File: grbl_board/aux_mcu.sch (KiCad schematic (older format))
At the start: 50 parts, among them J17 USB_B, J18 ICSP, Q5 BSS127S, Q6 BSS127S, Q7 BSS127S, SW2 SW_Push, U25 FT231XS, U26 40106, U27 74LS155, U28 ATmega328P-AU, U29 74LS153, U30 74LS153, Y2 16M

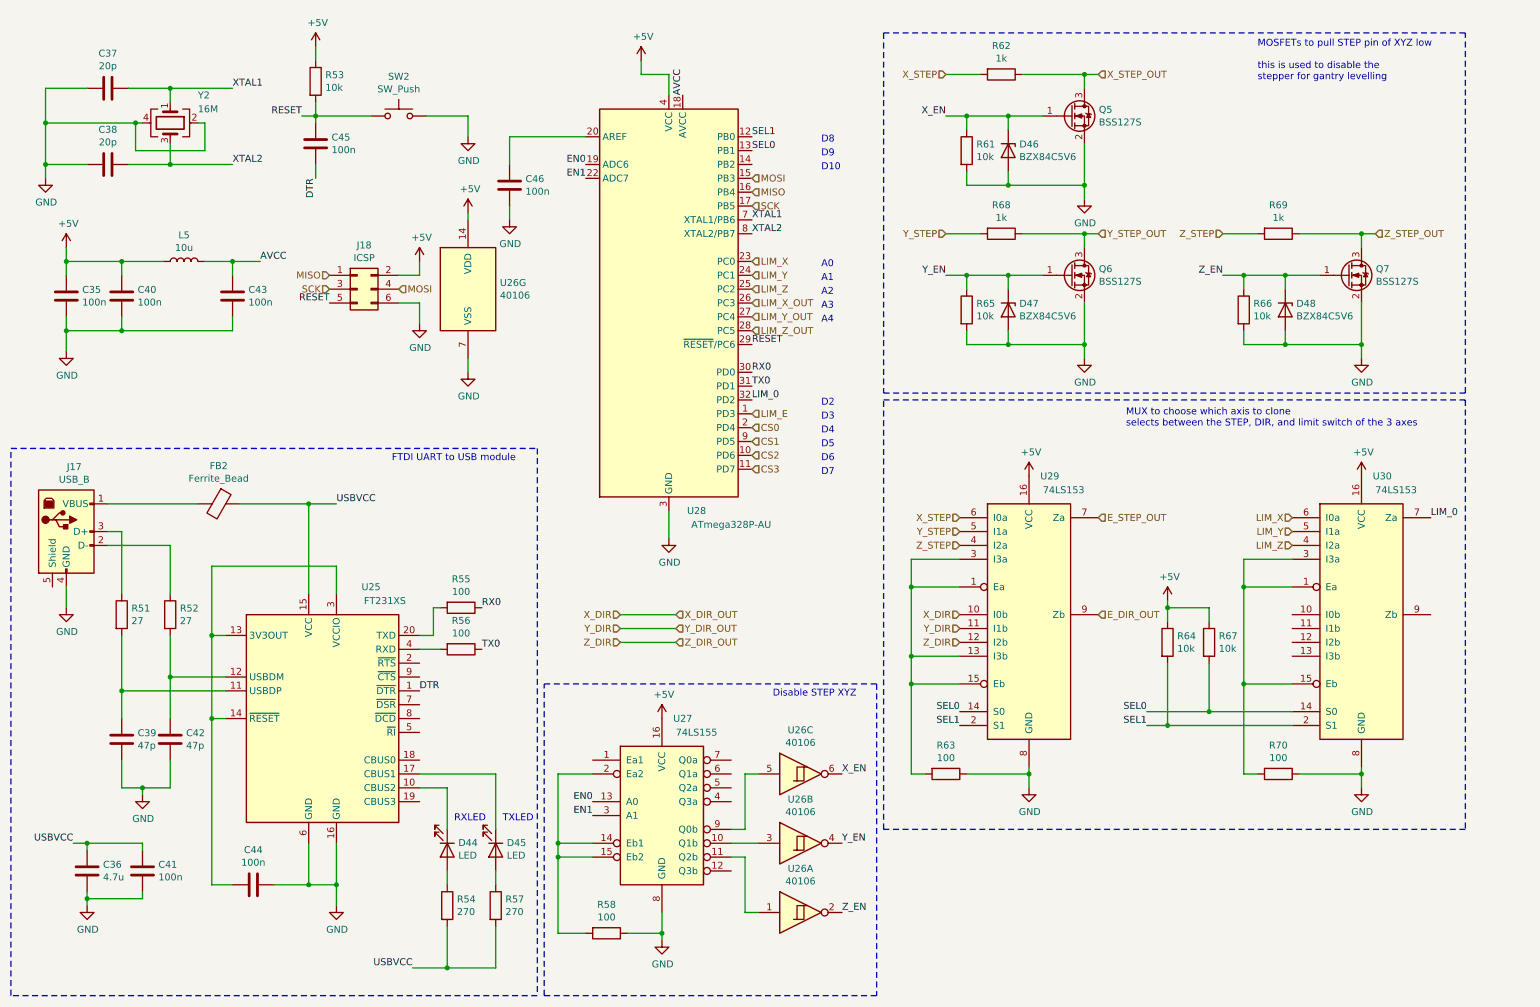
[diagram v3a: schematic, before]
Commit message: fixed limit switch disconnect issue
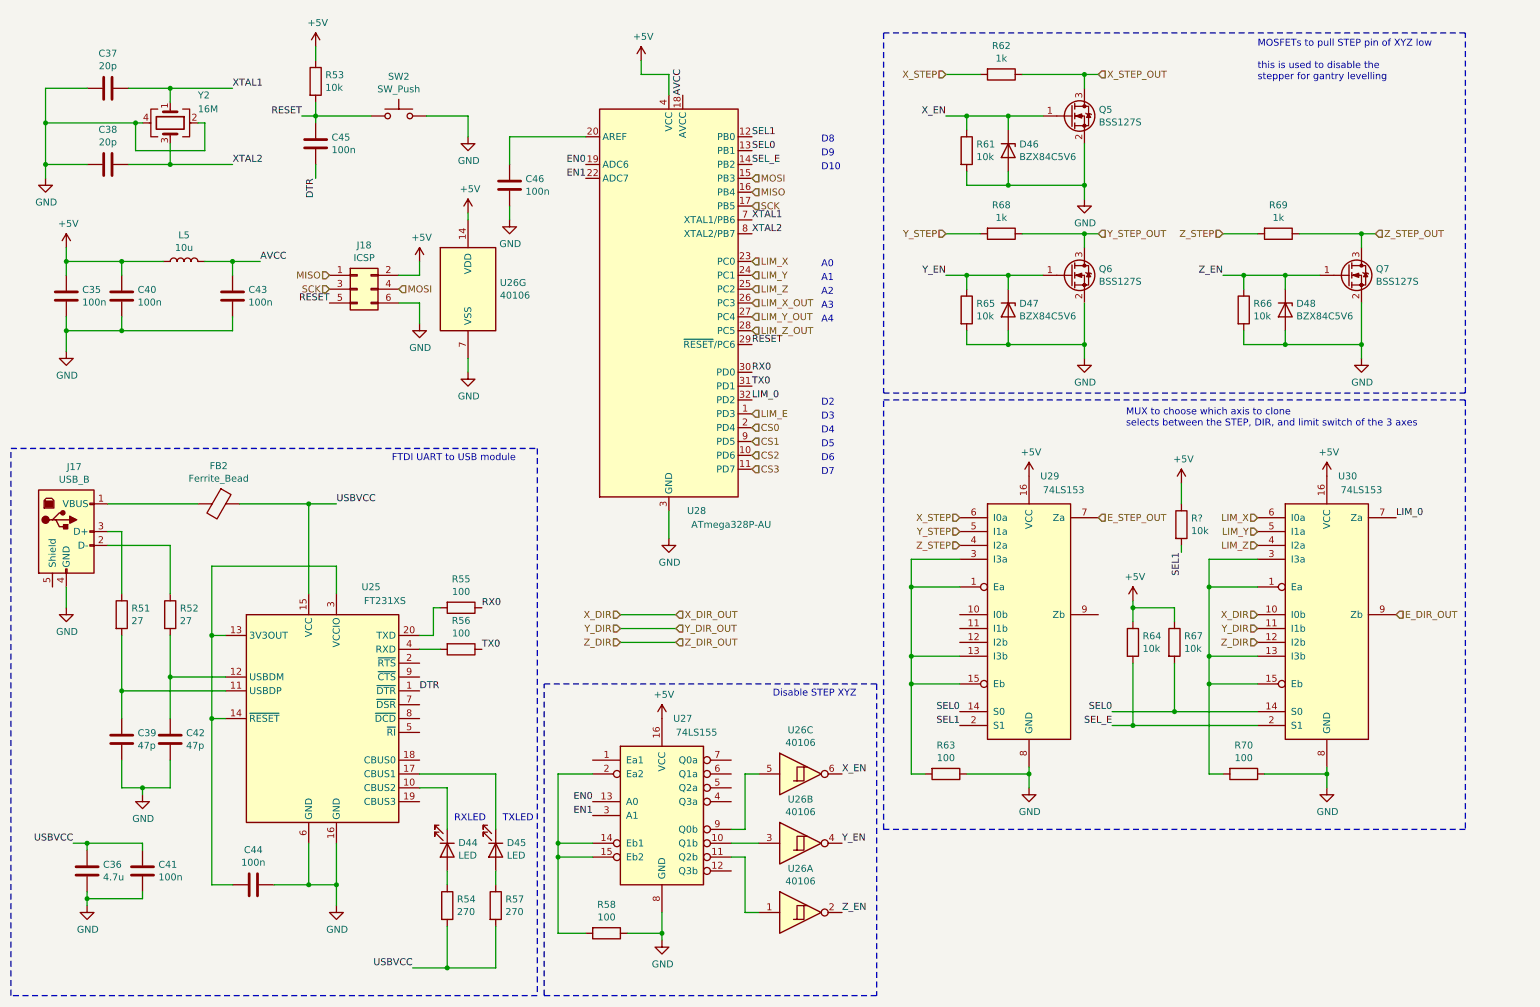
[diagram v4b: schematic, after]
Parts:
- added R?: 10k, Resistor_SMD:R_0805_2012Metric_Pad1.15x1.40mm_HandSolder, symbol Device:R
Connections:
- net +5V: now also R?.1
- net E_DIR_OUT: now also U30.9 (Zb); no longer U29.9 (Zb)
- net SEL1: now also R?.2; no longer R64.2, U30.2 (S1)
- net X_DIR: now also U30.10 (I0b); no longer U29.10 (I0b)
- net Y_DIR: now also U30.11 (I1b); no longer U29.11 (I1b)
- net Z_DIR: now also U30.12 (I2b); no longer U29.12 (I2b)
- net SEL_E: now reaches U28.14 (PB2)
- net SEL_E: now also R64.2, U30.2 (S1)
- net at R70.2, U30.1 (Ea), U30.15 (Eb)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: now also U30.13 (I3b)
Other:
- moved on the sheet: R64, R67, R70, U30
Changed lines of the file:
@@
 	1    0    0    -1
 $EndComp
-Text Label 10800 4200 0    50   ~ 0
+Text Label 10550 4200 0    50   ~ 0
 LIM_0
 Text Label 7400 5600 2    50   ~ 0
@@
 Wire Notes Line
 	4400 5400 6800 5400
-Connection ~ 9200 5600
-Connection ~ 8900 5700
+Connection ~ 8950 5600
+Connection ~ 8650 5700
 $Comp
 L Device:R R67
 U 1 1 61E49973
-P 9200 5100
-F 0 "R67" H 9270 5146 50  0000 L CNN
-F 1 "10k" H 9270 5055 50  0000 L CNN
-F 2 "Resistor_SMD:R_0805_2012Metric_Pad1.15x1.40mm_HandSolder" V 9130 5100 50  0001 C CNN
-F 3 "https://www.yageo.com/upload/media/product/productsearch/datasheet/rchip/PYu-RC_Group_51_RoHS_L_11.pdf" H 9200 5100 50  0001 C CNN
-F 4 "311-10KARCT-ND" H 9200 5100 50  0001 C CNN "Digikey Part No."
-	1    9200 5100
-	1    0    0    -1
-$EndComp
-Wire Wire Line
-	9200 5600 9200 5250
-Wire Wire Line
-	9200 5600 8750 5600
-Wire Wire Line
-	9200 5600 9800 5600
-Wire Wire Line
-	8900 4850 9200 4850
-Connection ~ 8900 4850
-Wire Wire Line
-	8900 4800 8900 4850
-Wire Wire Line
-	8900 4850 8900 4950
-Wire Wire Line
-	9200 4850 9200 4950
-Wire Wire Line
-	8900 5700 8900 5250
-Wire Wire Line
-	8750 5700 8900 5700
-Wire Wire Line
-	9800 5700 8900 5700
+P 8950 5100
+F 0 "R67" H 9020 5146 50  0000 L CNN
+F 1 "10k" H 9020 5055 50  0000 L CNN
+F 2 "Resistor_SMD:R_0805_2012Metric_Pad1.15x1.40mm_HandSolder" V 8880 5100 50  0001 C CNN
+F 3 "https://www.yageo.com/upload/media/product/productsearch/datasheet/rchip/PYu-RC_Group_51_RoHS_L_11.pdf" H 8950 5100 50  0001 C CNN
+F 4 "311-10KARCT-ND" H 8950 5100 50  0001 C CNN "Digikey Part No."
+	1    8950 5100
+	1    0    0    -1
+$EndComp
+Wire Wire Line
+	8950 5600 8950 5250
+Wire Wire Line
+	8950 5600 8500 5600
+Wire Wire Line
+	8950 5600 9550 5600
+Wire Wire Line
+	8650 4850 8950 4850
+Connection ~ 8650 4850
+Wire Wire Line
+	8650 4800 8650 4850
+Wire Wire Line
+	8650 4850 8650 4950
+Wire Wire Line
+	8950 4850 8950 4950
+Wire Wire Line
+	8650 5700 8650 5250
+Wire Wire Line
+	8500 5700 8650 5700
+Wire Wire Line
+	9550 5700 8650 5700
 $Comp
 L power:+5V #PWR099
 U 1 1 61E499A2
-P 8900 4800
-F 0 "#PWR099" H 8900 4650 50  0001 C CNN
-F 1 "+5V" H 8915 4973 50  0000 C CNN
-F 2 "" H 8900 4800 50  0001 C CNN
-F 3 "" H 8900 4800 50  0001 C CNN
-	1    8900 4800
+P 8650 4800
+F 0 "#PWR099" H 8650 4650 50  0001 C CNN
+F 1 "+5V" H 8665 4973 50  0000 C CNN
+F 2 "" H 8650 4800 50  0001 C CNN
+F 3 "" H 8650 4800 50  0001 C CNN
+	1    8650 4800
 	1    0    0    -1
 $EndComp
@@
 L Device:R R64
 U 1 1 61E499A8
-P 8900 5100
-F 0 "R64" H 8970 5146 50  0000 L CNN
-F 1 "10k" H 8970 5055 50  0000 L CNN
-F 2 "Resistor_SMD:R_0805_2012Metric_Pad1.15x1.40mm_HandSolder" V 8830 5100 50  0001 C CNN
-F 3 "https://www.yageo.com/upload/media/product/productsearch/datasheet/rchip/PYu-RC_Group_51_RoHS_L_11.pdf" H 8900 5100 50  0001 C CNN
-F 4 "311-10KARCT-ND" H 8900 5100 50  0001 C CNN "Digikey Part No."
-	1    8900 5100
+P 8650 5100
+F 0 "R64" H 8720 5146 50  0000 L CNN
+F 1 "10k" H 8720 5055 50  0000 L CNN
+F 2 "Resistor_SMD:R_0805_2012Metric_Pad1.15x1.40mm_HandSolder" V 8580 5100 50  0001 C CNN
+F 3 "https://www.yageo.com/upload/media/product/productsearch/datasheet/rchip/PYu-RC_Group_51_RoHS_L_11.pdf" H 8650 5100 50  0001 C CNN
+F 4 "311-10KARCT-ND" H 8650 5100 50  0001 C CNN "Digikey Part No."
+	1    8650 5100
 	1    0    0    -1
 $EndComp
 Text HLabel 8400 4200 2    50   Input ~ 0
 E_STEP_OUT
-Text Label 8750 5600 2    50   ~ 0
+Text Label 8500 5600 2    50   ~ 0
 SEL0
-Text Label 8750 5700 2    50   ~ 0
-SEL1
-Wire Wire Line
-	10300 6000 10300 6050
-Connection ~ 9450 4700
-Wire Wire Line
-	9450 4500 9450 4700
-Wire Wire Line
-	9800 4500 9450 4500
-Connection ~ 9450 5400
-Wire Wire Line
-	9800 5400 9450 5400
-Wire Wire Line
-	9450 4700 9800 4700
-Wire Wire Line
-	9450 6050 9450 5400
-Text HLabel 9800 4400 0    50   Input ~ 0
+Wire Wire Line
+	10050 6000 10050 6050
+Connection ~ 9200 4700
+Wire Wire Line
+	9200 4500 9200 4700
+Wire Wire Line
+	9550 4500 9200 4500
+Connection ~ 9200 5400
+Wire Wire Line
+	9550 5400 9200 5400
+Wire Wire Line
+	9200 4700 9550 4700
+Wire Wire Line
+	9200 6050 9200 5400
+Text HLabel 9550 4400 0    50   Input ~ 0
 LIM_Z
-Text HLabel 9800 4300 0    50   Input ~ 0
+Text HLabel 9550 4300 0    50   Input ~ 0
 LIM_Y
-Text HLabel 9800 4200 0    50   Input ~ 0
+Text HLabel 9550 4200 0    50   Input ~ 0
 LIM_X
 $Comp
 L 74xx:74LS153 U30
 U 1 1 61E49967
-P 10300 4900
-F 0 "U30" H 10450 5900 50  0000 C CNN
-F 1 "74LS153" H 10550 5800 50  0000 C CNN
-F 2 "Package_SO:SOIC-16_3.9x9.9mm_P1.27mm" H 10300 4900 50  0001 C CNN
-F 3 "http://www.ti.com/lit/gpn/sn74LS153" H 10300 4900 50  0001 C CNN
-F 4 "296-3653-5-ND" H 10300 4900 50  0001 C CNN "Digikey Part No."
-	1    10300 4900
-	1    0    0    -1
-$EndComp
-Text HLabel 8400 4900 2    50   Input ~ 0
-E_DIR_OUT
+P 10050 4900
+F 0 "U30" H 10200 5900 50  0000 C CNN
+F 1 "74LS153" H 10300 5800 50  0000 C CNN
+F 2 "Package_SO:SOIC-16_3.9x9.9mm_P1.27mm" H 10050 4900 50  0001 C CNN
+F 3 "http://www.ti.com/lit/gpn/sn74LS153" H 10050 4900 50  0001 C CNN
+F 4 "296-3653-5-ND" H 10050 4900 50  0001 C CNN "Digikey Part No."
+	1    10050 4900
+	1    0    0    -1
+$EndComp
 Wire Wire Line
 	7900 6050 7900 6150
@@
 	1    0    0    -1
 $EndComp
-Text HLabel 7400 5100 0    50   Input ~ 0
-Z_DIR
-Text HLabel 7400 5000 0    50   Input ~ 0
-Y_DIR
-Text HLabel 7400 4900 0    50   Input ~ 0
-X_DIR
 Text HLabel 7400 4400 0    50   Input ~ 0
 Z_STEP
@@
 L power:+5V #PWR0102
 U 1 1 61E8DDDC
-P 10300 3900
-F 0 "#PWR0102" H 10300 3750 50  0001 C CNN
-F 1 "+5V" H 10315 4073 50  0000 C CNN
-F 2 "" H 10300 3900 50  0001 C CNN
-F 3 "" H 10300 3900 50  0001 C CNN
-	1    10300 3900
-	1    0    0    -1
-$EndComp
-Wire Wire Line
-	9450 4700 9450 5400
-Connection ~ 10300 6050
+P 10050 3900
+F 0 "#PWR0102" H 10050 3750 50  0001 C CNN
+F 1 "+5V" H 10065 4073 50  0000 C CNN
+F 2 "" H 10050 3900 50  0001 C CNN
+F 3 "" H 10050 3900 50  0001 C CNN
+	1    10050 3900
+	1    0    0    -1
+$EndComp
+Wire Wire Line
+	9200 4700 9200 5200
+Connection ~ 10050 6050
 $Comp
 L power:GND #PWR0103
 U 1 1 61E4997C
-P 10300 6150
-F 0 "#PWR0103" H 10300 5900 50  0001 C CNN
-F 1 "GND" H 10305 5977 50  0000 C CNN
-F 2 "" H 10300 6150 50  0001 C CNN
-F 3 "" H 10300 6150 50  0001 C CNN
-	1    10300 6150
+P 10050 6150
+F 0 "#PWR0103" H 10050 5900 50  0001 C CNN
+F 1 "GND" H 10055 5977 50  0000 C CNN
+F 2 "" H 10050 6150 50  0001 C CNN
+F 3 "" H 10050 6150 50  0001 C CNN
+	1    10050 6150
 	1    0    0    -1
 $EndComp
@@
 L Device:R R70
 U 1 1 61E4998E
-P 9700 6050
-F 0 "R70" V 9493 6050 50  0000 C CNN
-F 1 "100" V 9584 6050 50  0000 C CNN
-F 2 "Resistor_SMD:R_0603_1608Metric_Pad0.98x0.95mm_HandSolder" V 9630 6050 50  0001 C CNN
-F 3 "https://www.yageo.com/upload/media/product/productsearch/datasheet/rchip/PYu-RC_Group_51_RoHS_L_11.pdf" H 9700 6050 50  0001 C CNN
-F 4 "311-100GRCT-ND" H 9700 6050 50  0001 C CNN "Digikey Part No."
-	1    9700 6050
+P 9450 6050
+F 0 "R70" V 9243 6050 50  0000 C CNN
+F 1 "100" V 9334 6050 50  0000 C CNN
+F 2 "Resistor_SMD:R_0603_1608Metric_Pad0.98x0.95mm_HandSolder" V 9380 6050 50  0001 C CNN
+F 3 "https://www.yageo.com/upload/media/product/productsearch/datasheet/rchip/PYu-RC_Group_51_RoHS_L_11.pdf" H 9450 6050 50  0001 C CNN
+F 4 "311-100GRCT-ND" H 9450 6050 50  0001 C CNN "Digikey Part No."
+	1    9450 6050
 	0    1    1    0
 $EndComp
 Wire Wire Line
-	9550 6050 9450 6050
-Wire Wire Line
-	9850 6050 10300 6050
-Wire Wire Line
-	10300 6050 10300 6150
+	9300 6050 9200 6050
+Wire Wire Line
+	9600 6050 10050 6050
+Wire Wire Line
+	10050 6050 10050 6150
 Text Notes 9550 1050 0    50   ~ 0
 MOSFETs to pull STEP pin of XYZ low\n\nthis is used to disable the \nstepper for gantry levelling\n
@@
 Text Notes 8600 3550 0    50   ~ 0
 MUX to choose which axis to clone\nselects between the STEP, DIR, and limit switch of the 3 axes
+Text Label 5900 1650 0    50   ~ 0
+SEL_E
+Text Label 8500 5700 2    50   ~ 0
+SEL_E
+Text Label 9000 4450 3    50   ~ 0
+SEL1
+$Comp
+L power:+5V #PWR?
+U 1 1 6188BB6E
+P 9000 3950
+F 0 "#PWR?" H 9000 3800 50  0001 C CNN
+F 1 "+5V" H 9015 4123 50  0000 C CNN
+F 2 "" H 9000 3950 50  0001 C CNN
+F 3 "" H 9000 3950 50  0001 C CNN
+	1    9000 3950
+	1    0    0    -1
+$EndComp
+$Comp
+L Device:R R?
+U 1 1 6188BB75
+P 9000 4250
+F 0 "R?" H 9070 4296 50  0000 L CNN
+F 1 "10k" H 9070 4205 50  0000 L CNN
+F 2 "Resistor_SMD:R_0805_2012Metric_Pad1.15x1.40mm_HandSolder" V 8930 4250 50  0001 C CNN
+F 3 "https://www.yageo.com/upload/media/product/productsearch/datasheet/rchip/PYu-RC_Group_51_RoHS_L_11.pdf" H 9000 4250 50  0001 C CNN
+F 4 "311-10KARCT-ND" H 9000 4250 50  0001 C CNN "Digikey Part No."
+	1    9000 4250
+	1    0    0    -1
+$EndComp
+Wire Wire Line
+	9000 4100 9000 3950
+Wire Wire Line
+	9000 4450 9000 4400
+Text HLabel 9550 5100 0    50   Input ~ 0
+Z_DIR
+Text HLabel 9550 5000 0    50   Input ~ 0
+Y_DIR
+Text HLabel 9550 4900 0    50   Input ~ 0
+X_DIR
+Wire Wire Line
+	9550 5200 9200 5200
+Connection ~ 9200 5200
+Wire Wire Line
+	9200 5200 9200 5400
+Text HLabel 10550 4900 2    50   Input ~ 0
+E_DIR_OUT
 $EndSCHEMATC

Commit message: fixed copper fill
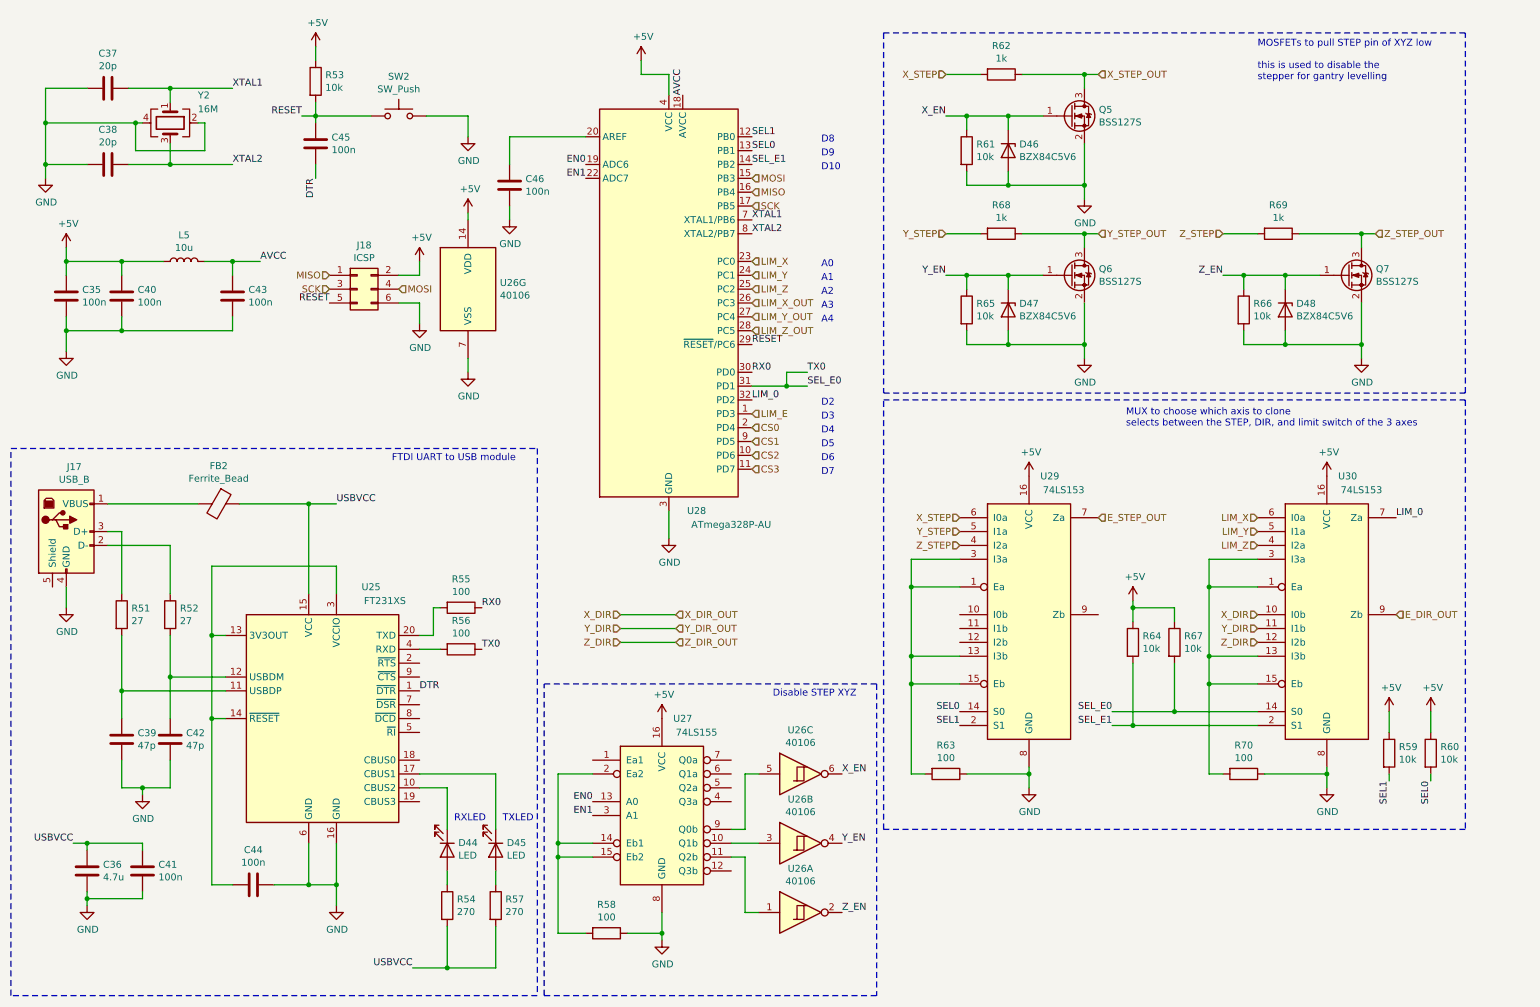
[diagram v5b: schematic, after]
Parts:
- added R60: 10k, Resistor_SMD:R_0805_2012Metric_Pad1.15x1.40mm_HandSolder, symbol Device:R
- gave numbers to parts that had none: 1
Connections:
- net +5V: now also R60.1
- net SEL0: now also R60.2; no longer R67.2, U30.14 (S0)
- net SEL_E renamed SEL_E1
- net TX0 renamed SEL_E0
- net SEL_E0: now also R67.2, U30.14 (S0)
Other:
- moved on the sheet: R59
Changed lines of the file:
@@
 Text Label 5900 3150 0    50   ~ 0
 RX0
-Text Label 5900 3250 0    50   ~ 0
+Text Label 6300 3150 0    50   ~ 0
 TX0
 Text Label 5900 2950 0    50   ~ 0
@@
 E_STEP_OUT
 Text Label 8500 5600 2    50   ~ 0
-SEL0
+SEL_E0
 Wire Wire Line
 	10050 6000 10050 6050
@@
 MUX to choose which axis to clone\nselects between the STEP, DIR, and limit switch of the 3 axes
 Text Label 5900 1650 0    50   ~ 0
-SEL_E
+SEL_E1
 Text Label 8500 5700 2    50   ~ 0
-SEL_E
-Text Label 9000 4450 3    50   ~ 0
+SEL_E1
+Text Label 10500 6100 3    50   ~ 0
 SEL1
 $Comp
-L power:+5V #PWR?
+L power:+5V #PWR0105
 U 1 1 6188BB6E
-P 9000 3950
-F 0 "#PWR?" H 9000 3800 50  0001 C CNN
-F 1 "+5V" H 9015 4123 50  0000 C CNN
-F 2 "" H 9000 3950 50  0001 C CNN
-F 3 "" H 9000 3950 50  0001 C CNN
-	1    9000 3950
-	1    0    0    -1
-$EndComp
-$Comp
-L Device:R R?
+P 10500 5600
+F 0 "#PWR0105" H 10500 5450 50  0001 C CNN
+F 1 "+5V" H 10515 5773 50  0000 C CNN
+F 2 "" H 10500 5600 50  0001 C CNN
+F 3 "" H 10500 5600 50  0001 C CNN
+	1    10500 5600
+	1    0    0    -1
+$EndComp
+$Comp
+L Device:R R59
 U 1 1 6188BB75
-P 9000 4250
-F 0 "R?" H 9070 4296 50  0000 L CNN
-F 1 "10k" H 9070 4205 50  0000 L CNN
-F 2 "Resistor_SMD:R_0805_2012Metric_Pad1.15x1.40mm_HandSolder" V 8930 4250 50  0001 C CNN
-F 3 "https://www.yageo.com/upload/media/product/productsearch/datasheet/rchip/PYu-RC_Group_51_RoHS_L_11.pdf" H 9000 4250 50  0001 C CNN
-F 4 "311-10KARCT-ND" H 9000 4250 50  0001 C CNN "Digikey Part No."
-	1    9000 4250
-	1    0    0    -1
-$EndComp
-Wire Wire Line
-	9000 4100 9000 3950
-Wire Wire Line
-	9000 4450 9000 4400
+P 10500 5900
+F 0 "R59" H 10570 5946 50  0000 L CNN
+F 1 "10k" H 10570 5855 50  0000 L CNN
+F 2 "Resistor_SMD:R_0805_2012Metric_Pad1.15x1.40mm_HandSolder" V 10430 5900 50  0001 C CNN
+F 3 "https://www.yageo.com/upload/media/product/productsearch/datasheet/rchip/PYu-RC_Group_51_RoHS_L_11.pdf" H 10500 5900 50  0001 C CNN
+F 4 "311-10KARCT-ND" H 10500 5900 50  0001 C CNN "Digikey Part No."
+	1    10500 5900
+	1    0    0    -1
+$EndComp
+Wire Wire Line
+	10500 5750 10500 5600
+Wire Wire Line
+	10500 6100 10500 6050
 Text HLabel 9550 5100 0    50   Input ~ 0
 Z_DIR
@@
 Text HLabel 10550 4900 2    50   Input ~ 0
 E_DIR_OUT
+Text Label 6300 3250 0    50   ~ 0
+SEL_E0
+Wire Wire Line
+	6300 3250 6150 3250
+Wire Wire Line
+	6300 3150 6150 3150
+Wire Wire Line
+	6150 3150 6150 3250
+Connection ~ 6150 3250
+Wire Wire Line
+	6150 3250 5900 3250
+Text Label 10800 6100 3    50   ~ 0
+SEL0
+$Comp
+L power:+5V #PWR095
+U 1 1 619E2203
+P 10800 5600
+F 0 "#PWR095" H 10800 5450 50  0001 C CNN
+F 1 "+5V" H 10815 5773 50  0000 C CNN
+F 2 "" H 10800 5600 50  0001 C CNN
+F 3 "" H 10800 5600 50  0001 C CNN
+	1    10800 5600
+	1    0    0    -1
+$EndComp
+$Comp
+L Device:R R60
+U 1 1 619E220A
+P 10800 5900
+F 0 "R60" H 10870 5946 50  0000 L CNN
+F 1 "10k" H 10870 5855 50  0000 L CNN
+F 2 "Resistor_SMD:R_0805_2012Metric_Pad1.15x1.40mm_HandSolder" V 10730 5900 50  0001 C CNN
+F 3 "https://www.yageo.com/upload/media/product/productsearch/datasheet/rchip/PYu-RC_Group_51_RoHS_L_11.pdf" H 10800 5900 50  0001 C CNN
+F 4 "311-10KARCT-ND" H 10800 5900 50  0001 C CNN "Digikey Part No."
+	1    10800 5900
+	1    0    0    -1
+$EndComp
+Wire Wire Line
+	10800 5750 10800 5600
+Wire Wire Line
+	10800 6100 10800 6050
 $EndSCHEMATC
